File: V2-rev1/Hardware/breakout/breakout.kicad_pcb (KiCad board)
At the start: 2 copper layers, 12 parts, among them J0 7SEG_12V, J1 Conn_D, J2 Conn_C, J3 Conn_E, J4 Conn_B, J5 Conn_F, J6 Conn_A, J7 Conn_G

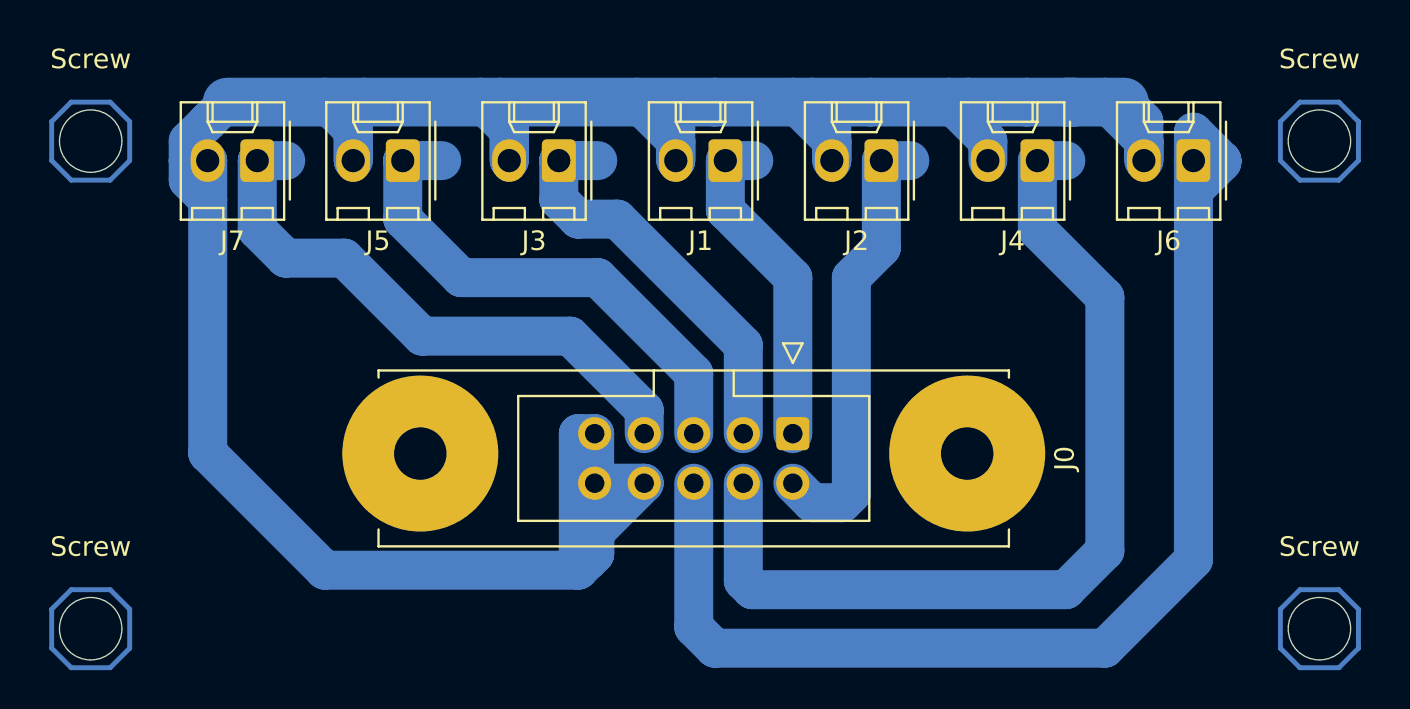
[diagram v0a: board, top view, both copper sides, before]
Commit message: reinforce some copper
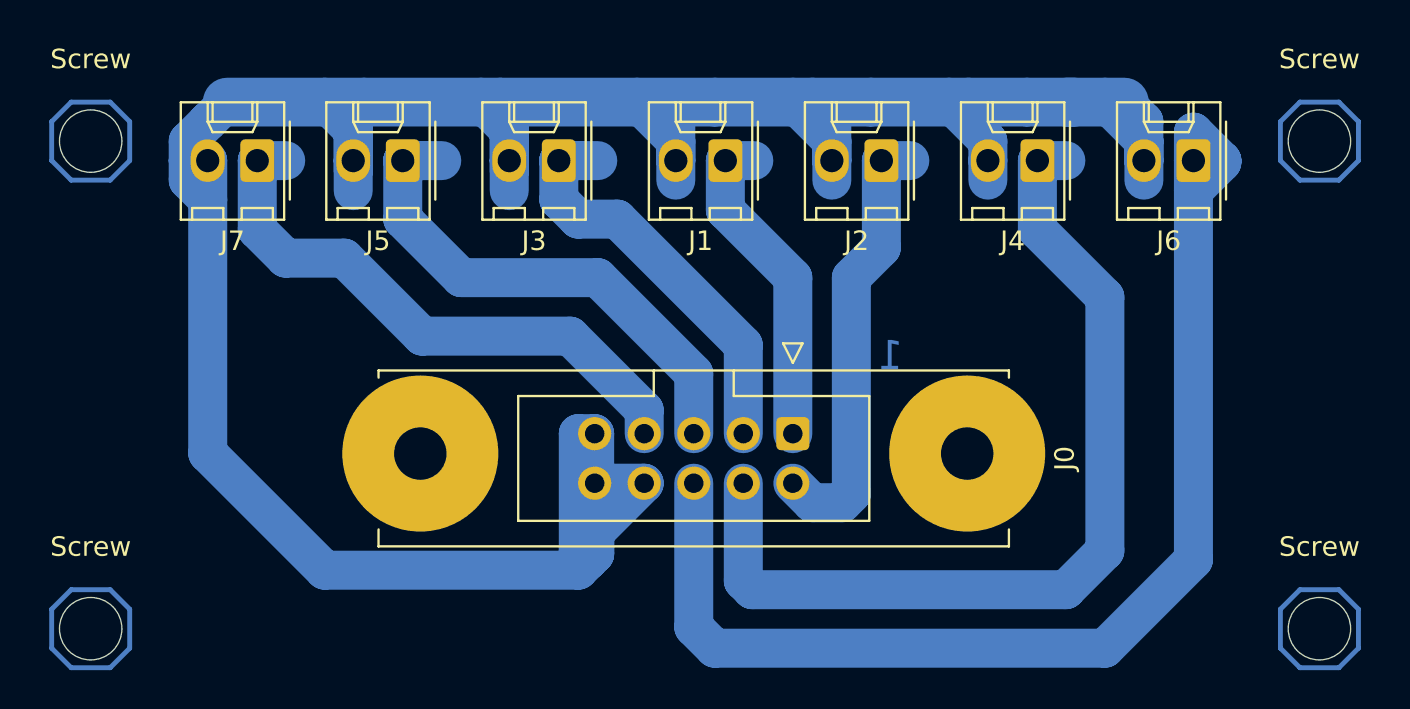
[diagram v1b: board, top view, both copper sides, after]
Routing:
- net /+12V: track 194.5 -> 202.7 mm
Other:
- board text added: "1"
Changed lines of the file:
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@@
   (general
     (thickness 1.6)
-    (drawings 6)
-    (tracks 156)
+    (drawings 7)
+    (tracks 164)
     (zones 0)
     (modules 12)
@@
       (rotate (xyz 0 0 0))
     )
+  )
+  (gr_text 1 (at 168 72) (layer B.Cu)
+    (effects (font (size 1.5 1.5) (thickness 0.3)) (justify mirror))
   )
   (gr_text "33 mm" (at 126 74) (layer Eco2.User)
@@
   (segment (start 152.84 81.08) (end 152.84 82.16) (width 2) (layer B.Cu) (net 8))
   (segment (start 155.38 78.54) (end 152.84 81.08) (width 2) (layer B.Cu) (net 8))
+  (segment (start 140.46 62) (end 140.46 62.54) (width 2) (layer B.Cu) (net 8))
+  (segment (start 148.46 62) (end 148.46 62.54) (width 2) (layer B.Cu) (net 8))
+  (segment (start 157 62) (end 157 63) (width 2) (layer B.Cu) (net 8))
+  (segment (start 165 62) (end 165 63) (width 2) (layer B.Cu) (net 8))
+  (segment (start 173 62) (end 173 63) (width 2) (layer B.Cu) (net 8))
+  (segment (start 181 62) (end 181 63) (width 2) (layer B.Cu) (net 8))
+  (segment (start 148.46 62) (end 148.46 63.54) (width 2) (layer B.Cu) (net 8))
+  (segment (start 140.46 62) (end 140.46 63.54) (width 2) (layer B.Cu) (net 8))
 )
